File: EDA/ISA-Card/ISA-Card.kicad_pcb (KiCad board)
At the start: 2 copper layers, 138.4 x 98.4 mm, 161 parts, among them U7101 74HCT245, U7102 74HCT244, U7104 74HCT138, U7105 74HCT138, U7106 74LS08, U7107 74LS32, U7108 74LS32, U7109 74HC368, U7110 74HC04, U7111 74HC125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

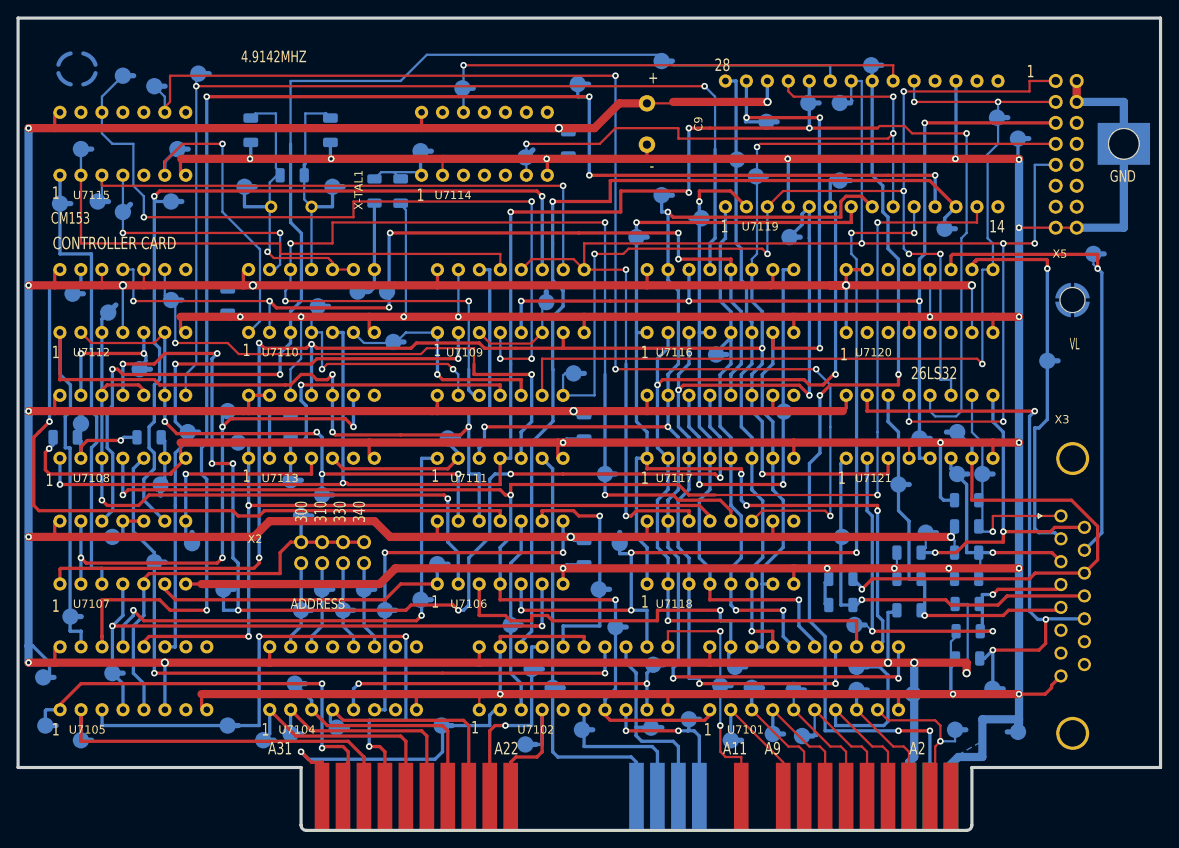
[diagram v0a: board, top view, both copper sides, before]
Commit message: Clean up SMD pad traces, change to hand solder pads to better match, and add missing models
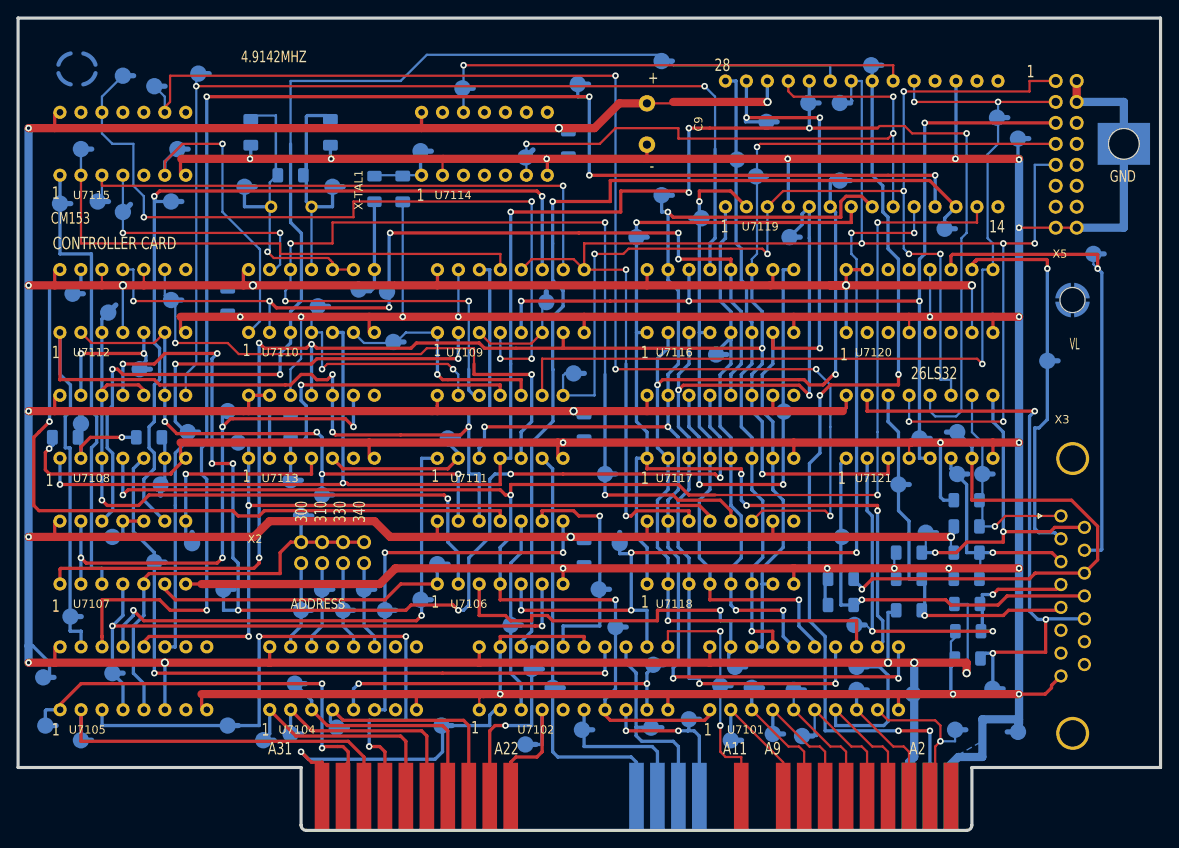
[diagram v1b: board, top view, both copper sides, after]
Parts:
- C1, C2, C3, C4, C5, C6, C7, C8: footprint Capacitor_SMD:C_1206_3216Metric -> Capacitor_SMD:C_1206_3216Metric_Pad1.33x1.80mm_HandSolder
- R1, R10, R11, R12, R13, R14, R15, R16, R2, R3, R4, R5, R6, R7, R8, R9: footprint Resistor_SMD:R_1206_3216Metric -> Resistor_SMD:R_1206_3216Metric_Pad1.30x1.75mm_HandSolder
- moved C7 0.36 mm to (119.0, 72.1)
- moved TP92 0.28 mm to (113.7, 84.3)
- moved C5 0.25 mm to (110.2, 65.3)
- moved C6 0.25 mm to (100.6, 65.3)
- moved R3 0.25 mm to (115.6, 72.1)
- moved R2 0.19 mm to (105.4, 70.5)
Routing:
- net Net-(C6-Pad2): track 38.4 -> 45.4 mm
- net /Response+: track 28.5 -> 26.8 mm
- net /Command-: track 58.4 -> 59.6 mm
- net Net-(C7-Pad1): track 10.3 -> 9.24 mm
- net Net-(C5-Pad2): track 27.6 -> 28.6 mm
- net Net-(TP95-Pad1): track 91.8 -> 92.8 mm

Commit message: All traces increased to 0.4mm minimum
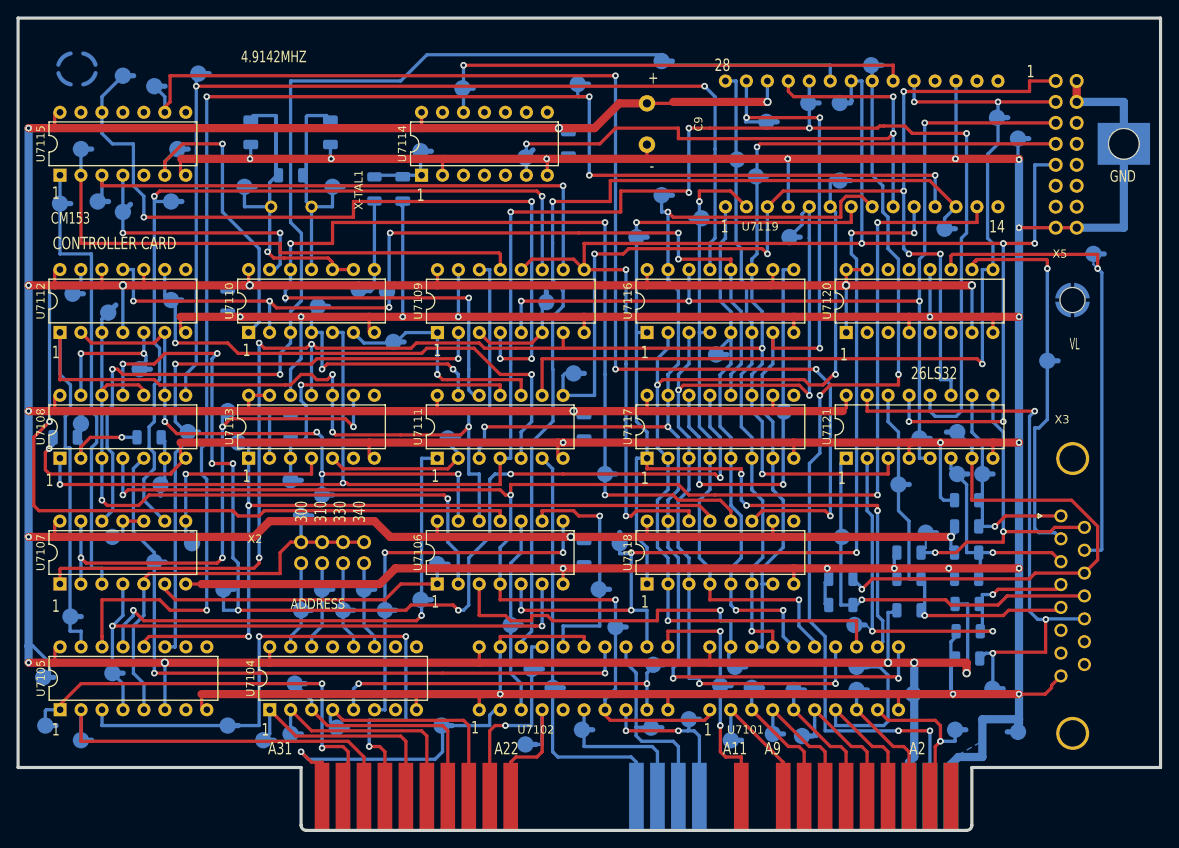
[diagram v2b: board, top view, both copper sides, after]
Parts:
- C1, C3, C8: value C -> 100nF; footprint Capacitor_SMD:C_1206_3216Metric_Pad1.33x1.80mm_HandSolder -> Capacitor_SMD:C_1206_3216Metric
- C2: value C -> 100uF; footprint Capacitor_SMD:C_1206_3216Metric_Pad1.33x1.80mm_HandSolder -> Capacitor_SMD:C_1206_3216Metric
- C4, C7: footprint Capacitor_SMD:C_1206_3216Metric_Pad1.33x1.80mm_HandSolder -> Capacitor_SMD:C_1206_3216Metric
- C5, C6: value C -> 14pF; footprint Capacitor_SMD:C_1206_3216Metric_Pad1.33x1.80mm_HandSolder -> Capacitor_SMD:C_1206_3216Metric
- R1, R10, R11, R12, R13, R14, R15, R16, R2, R3, R4, R5, R6, R7, R8, R9: footprint Resistor_SMD:R_1206_3216Metric_Pad1.30x1.75mm_HandSolder -> Resistor_SMD:R_1206_3216Metric
- U7104, U7105, U7109, U7116, U7117, U7118, U7120, U7121: footprint Philips-Shapes:DIP-16-Plain -> Package_DIP:DIP-16_W7.62mm
- U7106, U7107, U7108, U7110, U7111, U7112, U7113, U7114, U7115: footprint Philips-Shapes:DIP-14-Plain -> Package_DIP:DIP-14_W7.62mm
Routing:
- net Net-(TP96-Pad1): track 67.3 -> 65.4 mm

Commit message: Final cleanup complete
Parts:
- 7104: renamed from U7104; footprint Package_DIP:DIP-16_W7.62mm -> Philips-Shapes:DIP-16-Plain
- 7105: renamed from U7105; footprint Package_DIP:DIP-16_W7.62mm -> Philips-Shapes:DIP-16-Plain
- 7106: renamed from U7106; footprint Package_DIP:DIP-14_W7.62mm -> Philips-Shapes:DIP-14-Plain
- 7107: renamed from U7107; footprint Package_DIP:DIP-14_W7.62mm -> Philips-Shapes:DIP-14-Plain
- 7108: renamed from U7108; footprint Package_DIP:DIP-14_W7.62mm -> Philips-Shapes:DIP-14-Plain
- 7109: renamed from U7109; footprint Package_DIP:DIP-16_W7.62mm -> Philips-Shapes:DIP-16-Plain
- 7110: renamed from U7110; footprint Package_DIP:DIP-14_W7.62mm -> Philips-Shapes:DIP-14-Plain
- 7111: renamed from U7111; footprint Package_DIP:DIP-14_W7.62mm -> Philips-Shapes:DIP-14-Plain
- 7112: renamed from U7112; footprint Package_DIP:DIP-14_W7.62mm -> Philips-Shapes:DIP-14-Plain
- 7113: renamed from U7113; footprint Package_DIP:DIP-14_W7.62mm -> Philips-Shapes:DIP-14-Plain
- 7114: renamed from U7114; footprint Package_DIP:DIP-14_W7.62mm -> Philips-Shapes:DIP-14-Plain
- 7115: renamed from U7115; footprint Package_DIP:DIP-14_W7.62mm -> Philips-Shapes:DIP-14-Plain
- 7116: renamed from U7116; footprint Package_DIP:DIP-16_W7.62mm -> Philips-Shapes:DIP-16-Plain
- 7117: renamed from U7117; footprint Package_DIP:DIP-16_W7.62mm -> Philips-Shapes:DIP-16-Plain
- 7118: renamed from U7118; footprint Package_DIP:DIP-16_W7.62mm -> Philips-Shapes:DIP-16-Plain
- 7120: renamed from U7120; footprint Package_DIP:DIP-16_W7.62mm -> Philips-Shapes:DIP-16-Plain
- 7121: renamed from U7121; footprint Package_DIP:DIP-16_W7.62mm -> Philips-Shapes:DIP-16-Plain
- C1, C2, C3, C4, C5, C6, C7, C8: footprint Capacitor_SMD:C_1206_3216Metric -> Philips-Shapes:C_1206-Clean
- R1, R10, R11, R12, R13, R14, R15, R16, R2, R3, R4, R5, R6, R7, R8, R9: footprint Resistor_SMD:R_1206_3216Metric -> Philips-Shapes:R_1206-Clean
- renumbered U7101 to 7101, U7102 to 7102, U7119 to 7119, X-TAL1 to X-TAL
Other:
- board size 138.4 x 98.4 mm -> 137.5 x 96.9 mm

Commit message: Add attributtions
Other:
- board size 137.5 x 96.9 mm -> 138 x 96.9 mm
- board text added: "Helen_Croft"
- board text added: "Majenko"
- board text added: "Philips CM153 Clone By Shelby Jueden"
- board text added: "Special thanks to Roland for the original refrence photos"
- board text added: "With Help From:"
- board text added: "WizardTim"
- board text added: "https://github.com/AkBKukU/CM153-Repro"

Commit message: Adjust silk
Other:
- board text added: "Special thanks to original refrence Roland for the photos"
- board text removed: "Special thanks to Roland for the original refrence photos"
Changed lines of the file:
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@@
     (effects (font (size 1.6 1) (thickness 0.25)))
   )
-  (gr_text "Special thanks to     Roland for the\noriginal refrence      photos" (at 130.302 131.318) (layer "F.SilkS")
+  (gr_text "Special thanks to     original refrence\nRoland for the        photos" (at 130.302 131.318) (layer "F.SilkS")
     (effects (font (size 1.524 1.524) (thickness 0.3048)) (justify left))
   )

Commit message: Spelling is hard
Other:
- board text added: "Special thanks to original reference Roland for the photos"
- board text removed: "Special thanks to original refrence Roland for the photos"
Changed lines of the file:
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@@
     (effects (font (size 1.6 1) (thickness 0.25)))
   )
-  (gr_text "Special thanks to     original refrence\nRoland for the        photos" (at 130.302 131.318) (layer "F.SilkS")
+  (gr_text "Special thanks to     original reference\nRoland for the        photos" (at 130.302 131.318) (layer "F.SilkS")
     (effects (font (size 1.524 1.524) (thickness 0.3048)) (justify left))
   )

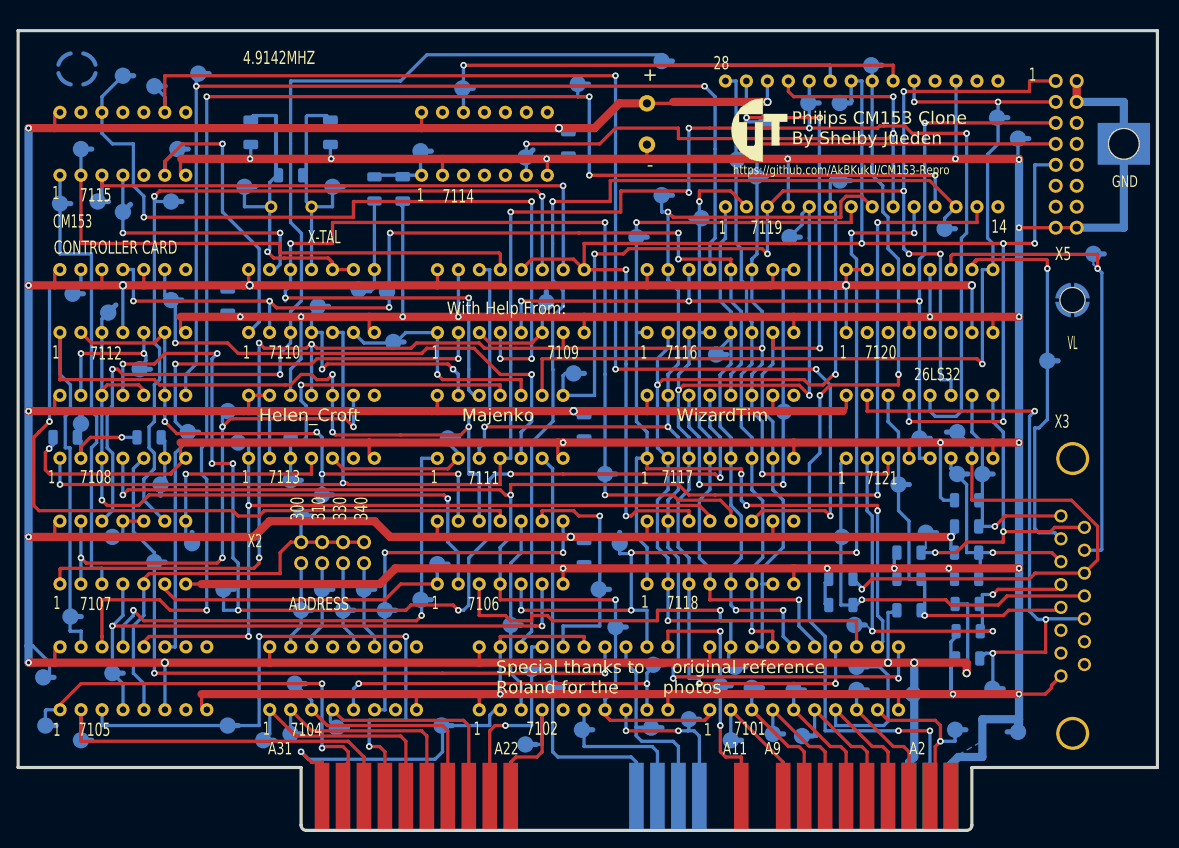
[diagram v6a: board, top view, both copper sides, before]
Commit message: minor trace cleanup
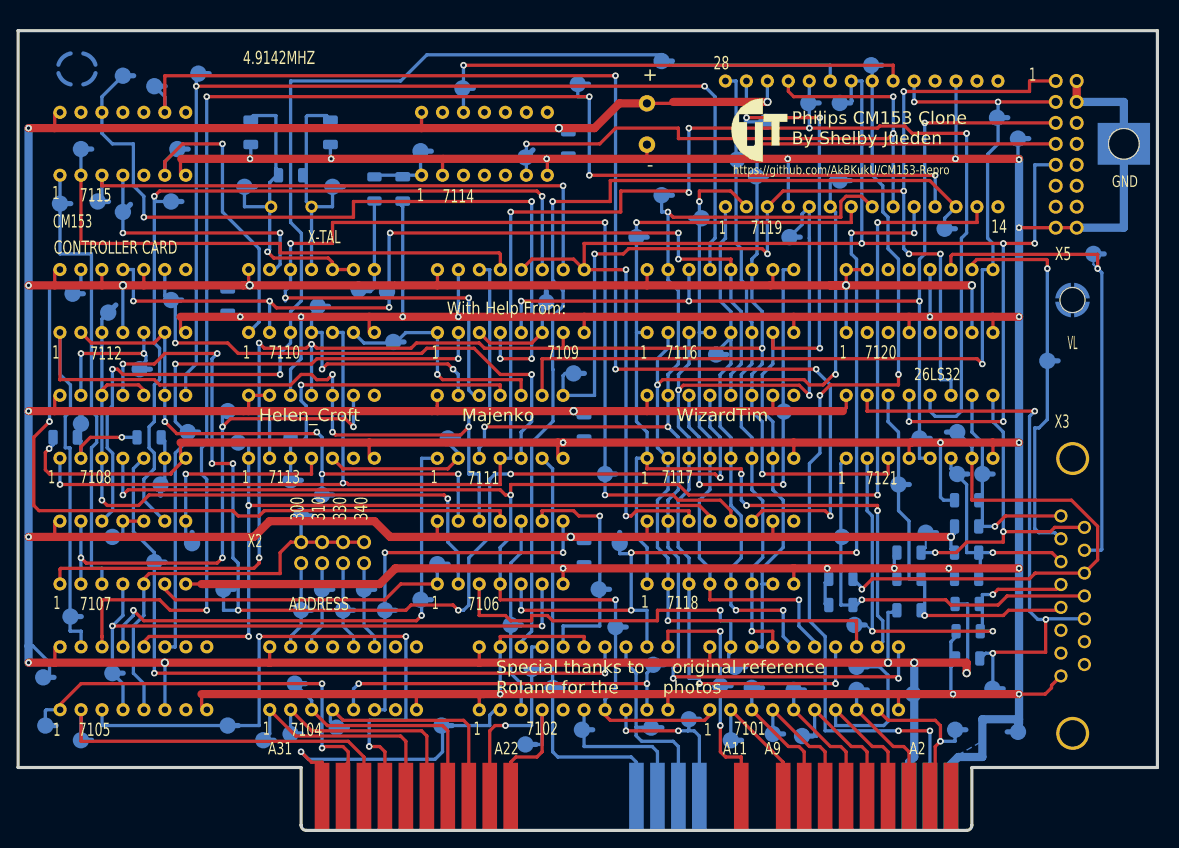
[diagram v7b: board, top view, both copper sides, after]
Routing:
- net Net-(C6-Pad2): track 45.4 -> 39.0 mm
- net GND: track 812.5 -> 809.4 mm
- net Net-(C5-Pad2): track 28.6 -> 26.9 mm
- net Net-(C7-Pad1): track 9.24 -> 8.54 mm

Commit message: Added mouser parts and card bracket
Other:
- board text added: "~55mm from bracket edge"
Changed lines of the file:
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@@
       (xy 162.6382 61.165986)
     ) (layer "F.SilkS") (width 0.01) (fill solid))
+  (gr_line (start 200.152 138.176) (end 219.71 138.176) (layer "Dwgs.User") (width 0.1))
+  (gr_line (start 210.82 49.53) (end 218.44 49.53) (layer "Dwgs.User") (width 0.1))
+  (gr_line (start 200.152 104.648) (end 219.71 104.648) (layer "Dwgs.User") (width 0.1))
+  (gr_line (start 212.344 49.784) (end 215.392 49.784) (layer "Dwgs.User") (width 0.1))
+  (gr_line (start 210.82 49.53) (end 210.82 156.21) (layer "Dwgs.User") (width 0.1))
+  (gr_line (start 212.344 104.394) (end 215.392 104.394) (layer "Dwgs.User") (width 0.1))
+  (gr_line (start 213.868 49.784) (end 213.868 104.394) (layer "Dwgs.User") (width 0.1))
   (gr_line (start 72.39 142.24) (end 106.68 142.24) (layer "Edge.Cuts") (width 0.381))
   (gr_arc (start 107.315 149.86) (mid 106.865987 149.674013) (end 106.68 149.225) (layer "Edge.Cuts") (width 0.381))
@@
     (effects (font (size 1.1 0.9) (thickness 0.2)) (justify left))
   )
+  (gr_text "~55mm from bracket edge" (at 215.138 75.946 90) (layer "Dwgs.User")
+    (effects (font (size 1 1) (thickness 0.15)))
+  )
   (segment (start 107.95 141.605) (end 106.68 140.335) (width 0.4) (layer "F.Cu") (net 1))
